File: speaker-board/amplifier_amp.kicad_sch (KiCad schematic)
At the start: 47 parts, among them J1 TPA3245DDVR

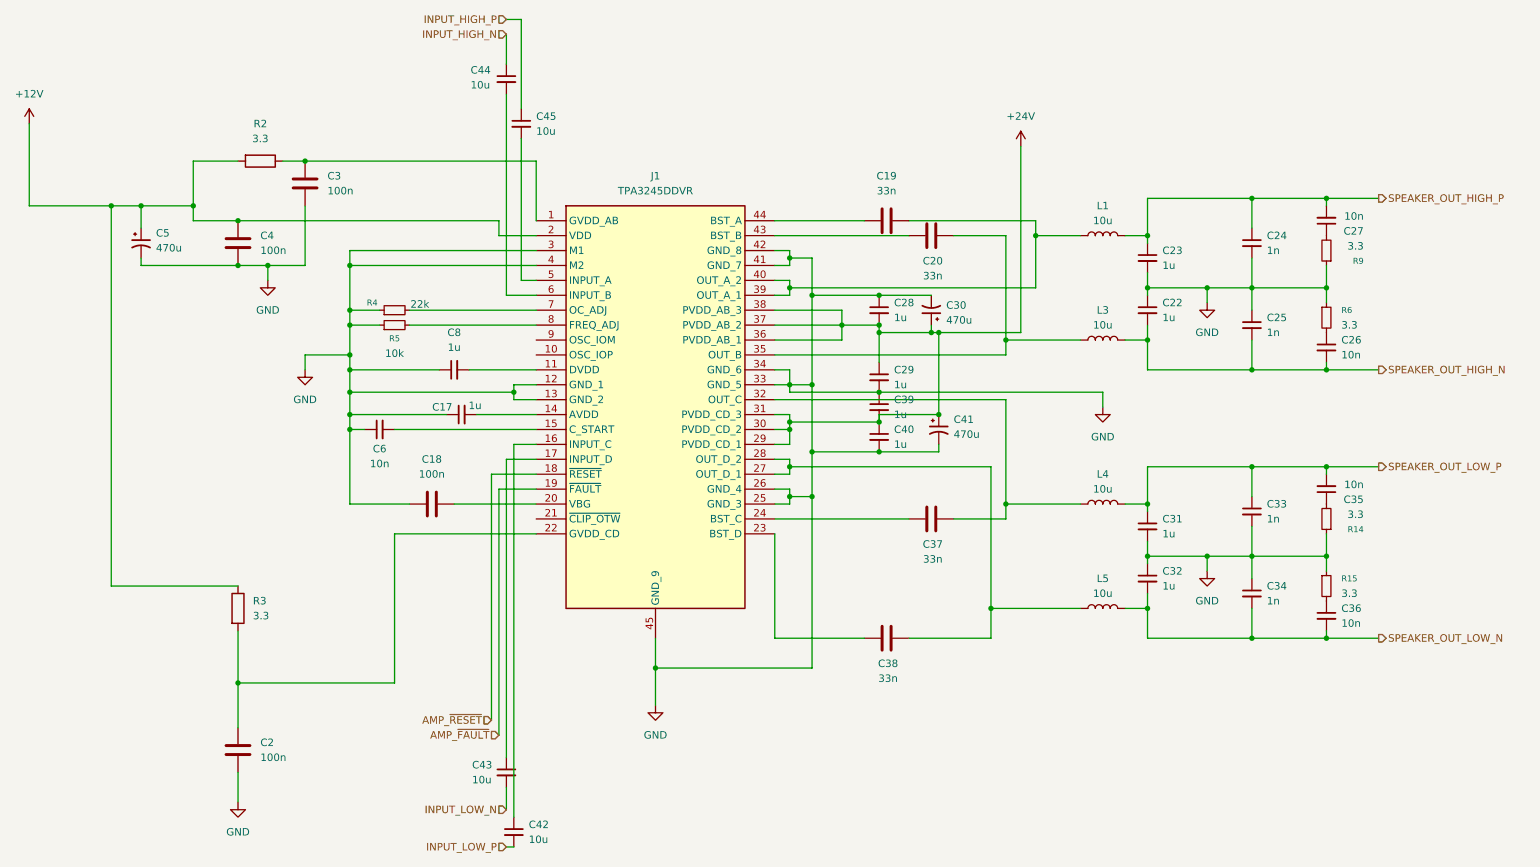
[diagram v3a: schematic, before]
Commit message: spec most parts for the amp
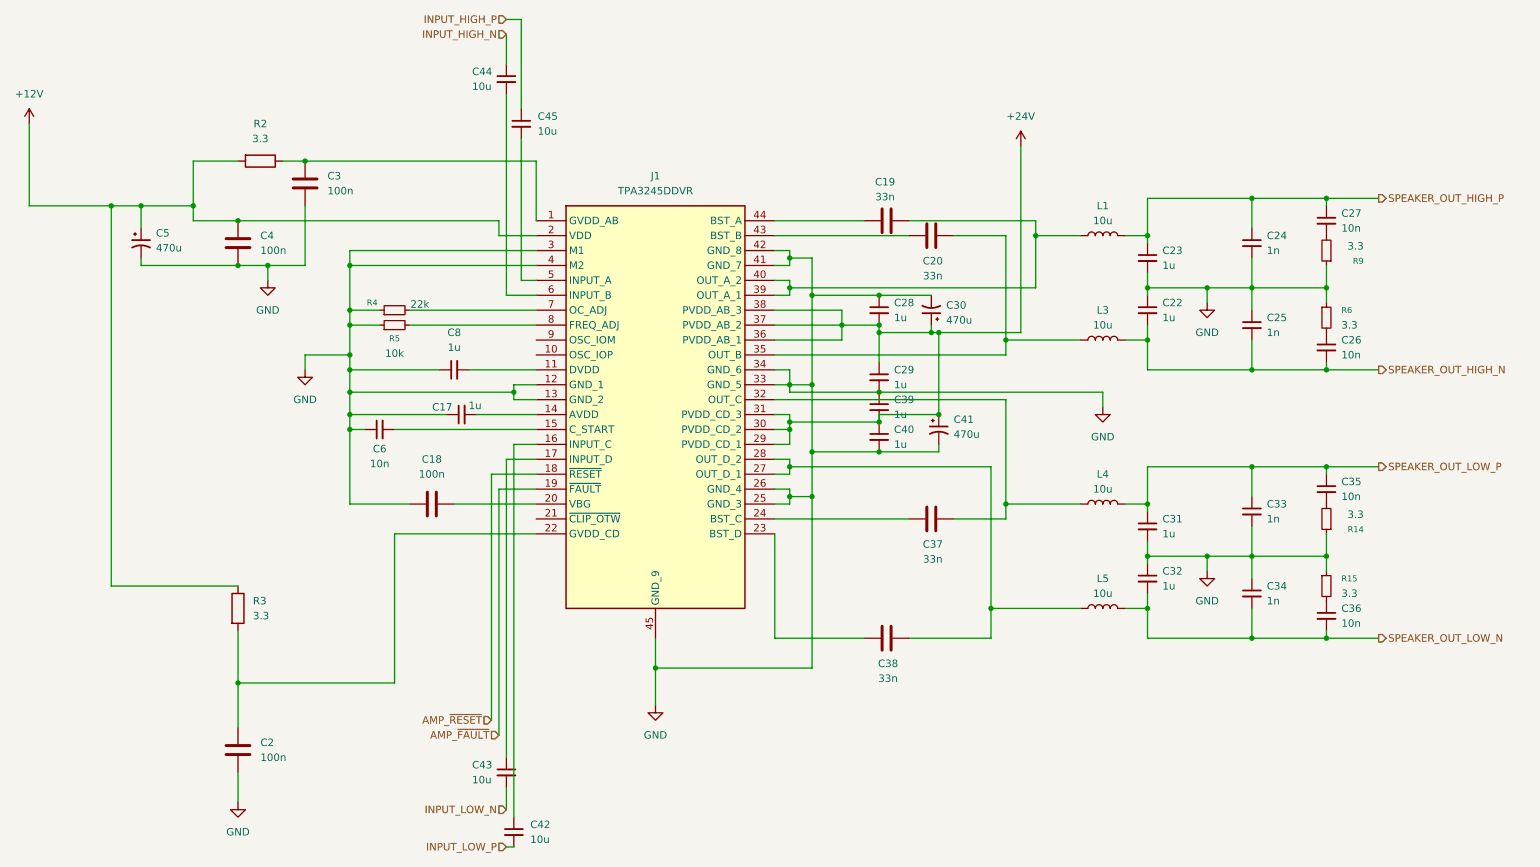
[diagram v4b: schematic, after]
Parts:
- C19, C20, C37, C38: Digikey Link (none) -> https://www.digikey.com/en/products/detail/kemet/C0805C333K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; Part # (none) -> C0805C333K5RECAUTO
- C22, C23, C31, C32: Digikey Link (none) -> https://www.digikey.com/en/products/detail/panasonic-electr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; Part # (none) -> ECW-FE2W105K
- C24, C25, C33, C34: Digikey Link (none) -> https://www.digikey.com/en/products/detail/kemet/C0805C102J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; Part # (none) -> C0805C102J5GACTU
- C26, C27, C35, C36: Digikey Link (none) -> https://www.digikey.com/en/products/detail/murata-electroni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; Part # (none) -> GRM1885C1H103JA01D
- C30, C41: Digikey Link (none) -> https://www.digikey.com/en/products/detail/kemet/ESY477M035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; Part # (none) -> ESY477M035AH4AA
- C42, C43, C44, C45: Digikey Link (none) -> https://www.digikey.com/en/products/detail/nichicon/UCL1V10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; Part # (none) -> UCL1V100MCL1GS
- C5: Digkey Link (none) -> https://www.digikey.com/en/products/detail/kemet/ESY477M035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; Part # (none) -> ESY477M035AH4AA
- L1, L3, L4, L5: Digikey Link (none) -> https://www.digikey.com/en/products/detail/sumida-america-i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; Part # (none) -> CDEP147NP-100MC-125
- R14, R15, R6, R9: Digikey Link (none) -> https://www.digikey.com/en/products/detail/vishay-dale/RCS1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; Part # (none) -> RCS12063R30FKEA
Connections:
- net SPEAKER_OUT_HIGH_P: now also C27.1; no longer C27.2
- net SPEAKER_OUT_LOW_P: now also C35.1; no longer C35.2
- net at R9.2: now also C27.2; no longer C27.1
- net at R14.2: now also C35.2; no longer C35.1

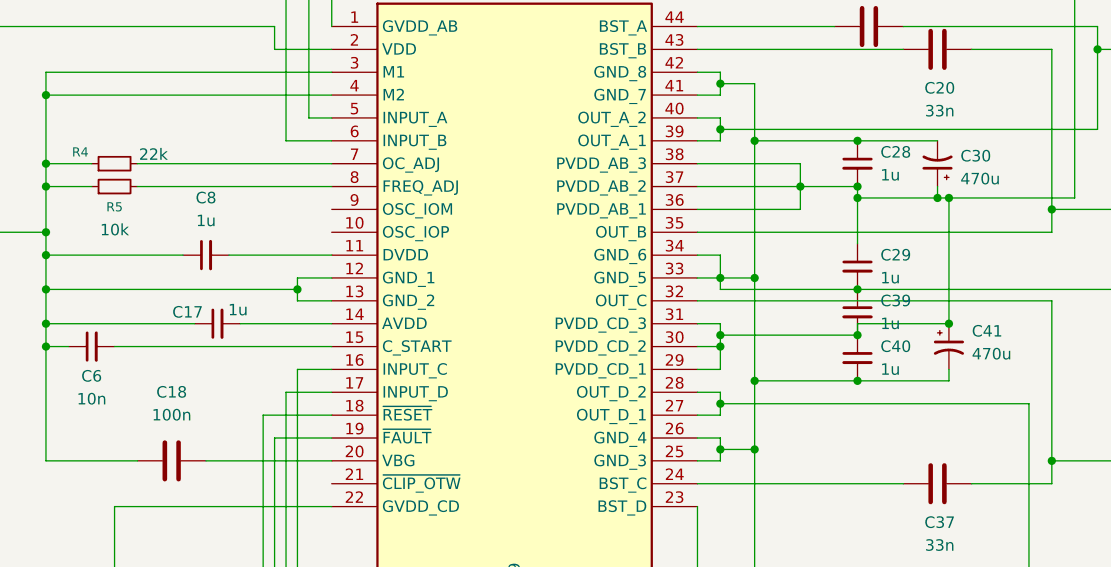
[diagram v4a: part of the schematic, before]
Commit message: add all amp parts
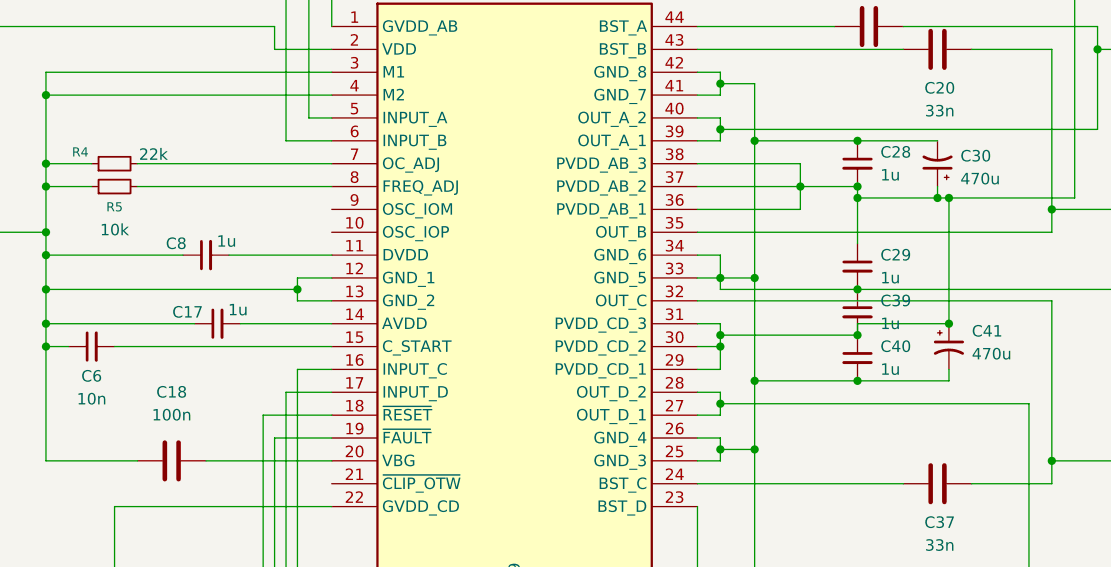
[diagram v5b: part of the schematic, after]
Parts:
- C17, C28, C29, C39, C40, C8: Digikey Link (none) -> https://www.digikey.com/en/products/detail/samsung-electro-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; Part # (none) -> CL31B105KBHNNNE
- C18, C2, C3, C4: Digikey Link (none) -> https://www.digikey.com/en/products/detail/kemet/C0603C104K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; Part # (none) -> C0603C104K5RACTU
- C6: Digikey Link (none) -> https://www.digikey.com/en/products/detail/kemet/C0603C103K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; Part # (none) -> C0603C103K5RACTU
- R2, R3: Digikey Link (none) -> https://www.digikey.com/en/products/detail/vishay-dale/RCS1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; Part # (none) -> RCS12063R30FKEA
- R4: Digikey Link (none) -> https://www.digikey.com/en/products/detail/vishay-dale-thin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; Part # (none) -> PHPA1206E2202BST1
- R5: Digikey Link (none) -> https://www.digikey.com/en/products/detail/vishay-dale-thin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; Part # (none) -> PHP01206E1002BST5

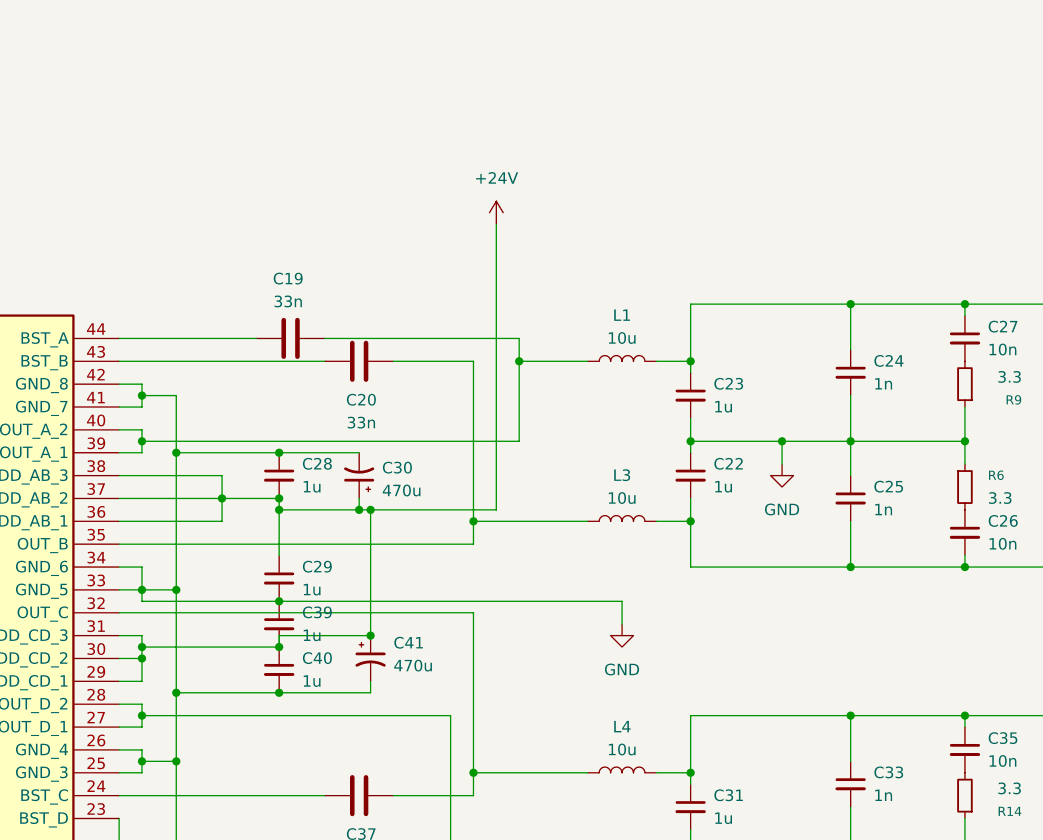
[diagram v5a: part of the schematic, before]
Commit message: upsizing power rial caps
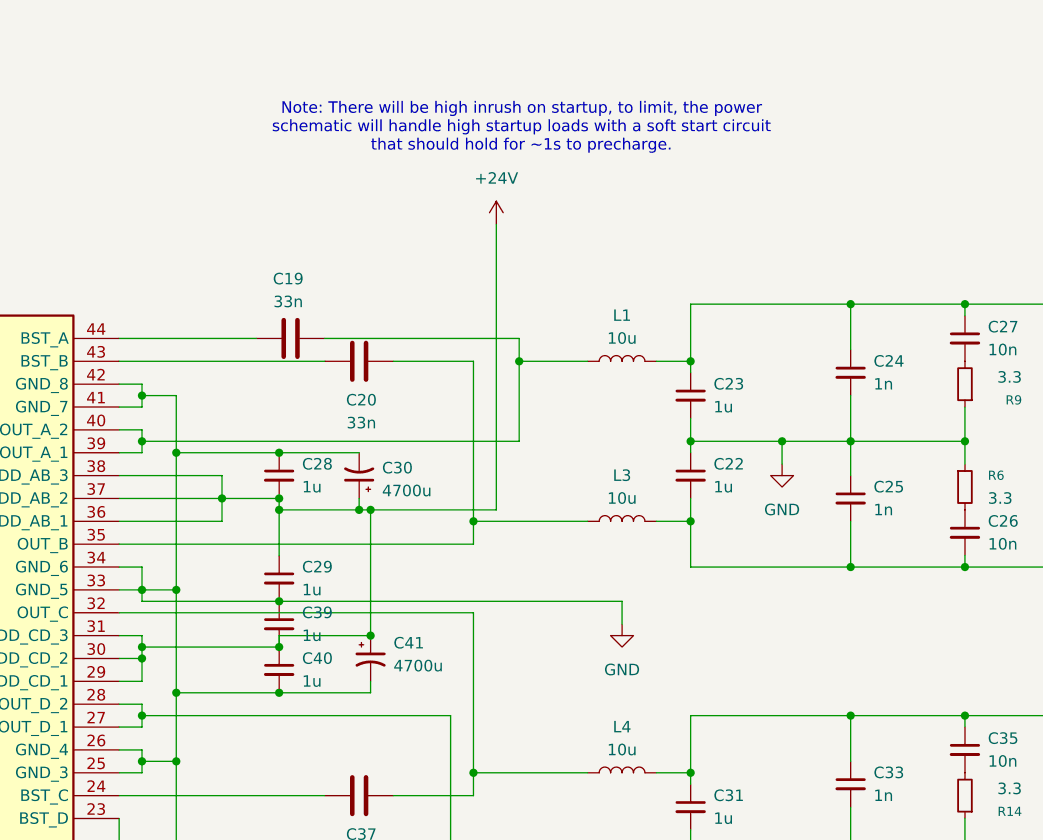
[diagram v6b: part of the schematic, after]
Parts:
- C30, C41: value 470u -> 4700u; Digikey Link https://www.digikey.com/en/products/detail/kemet/ESY477M035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 -> https://www.digikey.com/en/products/detail/rubycon/50PK4700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; Part # ESY477M035AH4AA -> 50PK4700MEFC18X40
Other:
- note added: "Note: There will be high inrush on startup, to limit, the power schematic will handle high startup loads with a soft start circuit that should hold for ~1s to precharge."
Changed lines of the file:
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@@
 		(company "Dhairya Gupta & Charan Pradeep")
+	)
+	(text "Note: There will be high inrush on startup, to limit, the power\nschematic will handle high startup loads with a soft start circuit\nthat should hold for ~1s to precharge."
+		(exclude_from_sim no)
+		(at 203.454 41.402 0)
+		(effects
+			(font
+				(size 1.27 1.27)
+			)
+		)
 	)
 	(junction
@@
 			)
 		)
-		(property "Value" "470u"
+		(property "Value" "4700u"
 			(at 187.96 81.7117 0)
 			(effects
@@
 			)
 		)
-		(property "Part #" "ESY477M035AH4AA"
+		(property "Part #" "50PK4700MEFC18X40"
 			(at 185.42 80.01 0)
 			(effects
@@
 			)
 		)
-		(property "Digikey Link" "https://www.digikey.com/en/products/detail/kemet/ESY477M035AH4AA/2712534"
+		(property "Digikey Link" "https://www.digikey.com/en/products/detail/rubycon/50PK4700MEFC18X40/3134353"
 			(at 185.42 80.01 0)
 			(effects
@@
 			)
 		)
-		(property "Value" "470u"
+		(property "Value" "4700u"
 			(at 189.23 101.1681 0)
 			(effects
@@
 			)
 		)
-		(property "Part #" "ESY477M035AH4AA"
+		(property "Part #" "50PK4700MEFC18X40"
 			(at 186.69 100.33 0)
 			(effects
@@
 			)
 		)
-		(property "Digikey Link" "https://www.digikey.com/en/products/detail/kemet/ESY477M035AH4AA/2712534"
+		(property "Digikey Link" "https://www.digikey.com/en/products/detail/rubycon/50PK4700MEFC18X40/3134353"
 			(at 186.69 100.33 0)
 			(effects

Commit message: add footprints
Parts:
- C17, C28, C29, C39, C40, C8: footprint (none) -> Capacitor_SMD:C_1206_3216Metric_Pad1.33x1.80mm_HandSolder
- C30, C41: footprint (none) -> Capacitor_THT:CP_Radial_D18.0mm_P7.50mm
- R14, R15, R2, R3, R4, R5, R6, R9: footprint (none) -> Resistor_SMD:R_1206_3216Metric_Pad1.30x1.75mm_HandSolder
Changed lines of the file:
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@@
 			)
 		)
-		(property "Footprint" ""
+		(property "Footprint" "Capacitor_THT:CP_Radial_D18.0mm_P7.50mm"
 			(at 185.42 80.01 0)
 			(effects
@@
 			)
 		)
-		(property "Footprint" ""
+		(property "Footprint" "Capacitor_THT:CP_Radial_D18.0mm_P7.50mm"
 			(at 186.69 100.33 0)
 			(effects
@@
 			)
 		)
-		(property "Footprint" ""
+		(property "Footprint" "Capacitor_SMD:C_1206_3216Metric_Pad1.33x1.80mm_HandSolder"
 			(at 176.53 96.52 0)
 			(effects
@@
 			)
 		)
-		(property "Footprint" ""
+		(property "Footprint" "Resistor_SMD:R_1206_3216Metric_Pad1.30x1.75mm_HandSolder"
 			(at 65.532 130.81 90)
 			(effects
@@
 			)
 		)
-		(property "Footprint" ""
+		(property "Footprint" "Resistor_SMD:R_1206_3216Metric_Pad1.30x1.75mm_HandSolder"
 			(at 93.98 80.01 0)
 			(effects
@@
 			)
 		)
-		(property "Footprint" ""
+		(property "Footprint" "Capacitor_SMD:C_1206_3216Metric_Pad1.33x1.80mm_HandSolder"
 			(at 176.53 101.6 0)
 			(effects
@@
 			)
 		)
-		(property "Footprint" ""
+		(property "Footprint" "Resistor_SMD:R_1206_3216Metric_Pad1.30x1.75mm_HandSolder"
 			(at 93.98 82.55 0)
 			(effects
@@
 			)
 		)
-		(property "Footprint" ""
+		(property "Footprint" "Resistor_SMD:R_1206_3216Metric_Pad1.30x1.75mm_HandSolder"
 			(at 252.73 69.85 0)
 			(effects
@@
 			)
 		)
-		(property "Footprint" ""
+		(property "Footprint" "Capacitor_SMD:C_1206_3216Metric_Pad1.33x1.80mm_HandSolder"
 			(at 105.41 97.79 0)
 			(effects
@@
 			)
 		)
-		(property "Footprint" ""
+		(property "Footprint" "Resistor_SMD:R_1206_3216Metric_Pad1.30x1.75mm_HandSolder"
 			(at 252.73 115.57 0)
 			(effects
@@
 			)
 		)
-		(property "Footprint" ""
+		(property "Footprint" "Resistor_SMD:R_1206_3216Metric_Pad1.30x1.75mm_HandSolder"
 			(at 252.73 81.28 0)
 			(effects
@@
 			)
 		)
-		(property "Footprint" ""
+		(property "Footprint" "Capacitor_SMD:C_1206_3216Metric_Pad1.33x1.80mm_HandSolder"
 			(at 176.53 80.01 0)
 			(effects
@@
 			)
 		)
-		(property "Footprint" ""
+		(property "Footprint" "Capacitor_SMD:C_1206_3216Metric_Pad1.33x1.80mm_HandSolder"
 			(at 176.53 91.44 0)
 			(effects
@@
 			)
 		)
-		(property "Footprint" ""
+		(property "Footprint" "Capacitor_SMD:C_1206_3216Metric_Pad1.33x1.80mm_HandSolder"
 			(at 104.14 90.17 0)
 			(effects
@@
 			)
 		)
-		(property "Footprint" ""
+		(property "Footprint" "Resistor_SMD:R_1206_3216Metric_Pad1.30x1.75mm_HandSolder"
 			(at 71.12 52.832 90)
 			(effects
@@
 			)
 		)
-		(property "Footprint" ""
+		(property "Footprint" "Resistor_SMD:R_1206_3216Metric_Pad1.30x1.75mm_HandSolder"
 			(at 252.73 127 0)
 			(effects
